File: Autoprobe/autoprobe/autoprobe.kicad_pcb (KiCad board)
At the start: 2 copper layers, 40.2 x 23.9 mm, 15 parts, among them J1 Conn_01x09, J2 Conn_01x05, J3 Molex 502494-0470, U1 M24C02-FMN

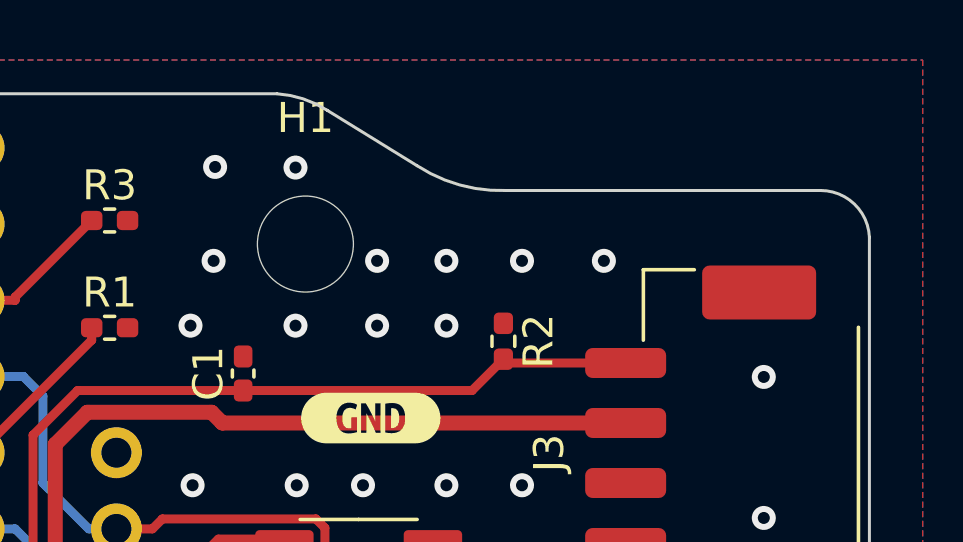
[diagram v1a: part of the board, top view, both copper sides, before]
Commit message: Update Autoprobe project to the Kicad 9.xx Add some Bin files for the EEPROM data add some documentation files
Update the High speed diff probe Kicad data
change the silkscreen - more reasonable position
Add the Project Name, an revision on the PCB board.
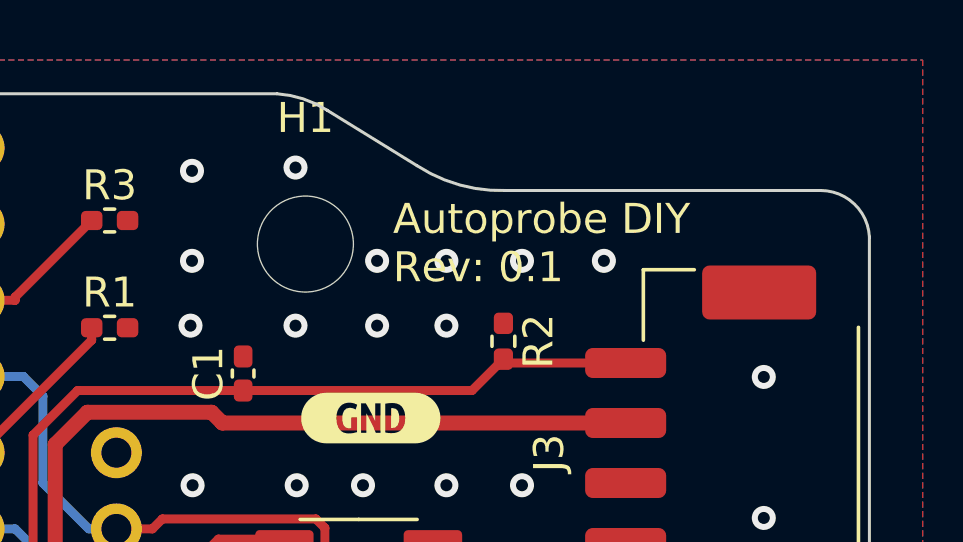
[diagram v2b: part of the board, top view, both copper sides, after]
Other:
- rule pad_to_mask_clearance: 0 -> 0.1
- board text added: "${TITLE} Rev: ${REVISION}"
